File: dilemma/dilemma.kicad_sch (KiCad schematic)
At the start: 64 parts, among them J1 S3B-PH-SM4-TB(LF)(SN), J2 Serial, J3 BATTERY_CONN_DEANS, J5 S3B-PH-SM4-TB(LF)(SN), J7 trackball, SW1 SW_Push, SW10 SW_Push, SW11 SW_Push, SW12 SW_Push, SW13 SW_Push, SW14 SW_Push, SW15 SW_Push, SW16 SW_Push, SW17 SW_Push, SW2 SW_Push, SW26 SW_SPST, SW3 SW_Push, SW37 SW_SPST, SW4 SW_Push, SW5 SW_Push, SW6 SW_Push, SW7 SW_Push, SW8 SW_Push, SW9 SW_Push, U2 eliteC

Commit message: routing routing routing
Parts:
- removed H3: M4, footprints:MountingHole_3mm_Pad_thin, symbol Mechanical:MountingHole_Pad
- added R1: 5.1k, footprints:R_1206_handsolder, symbol Device:R
- R7: footprint footprints:R_1206_handsolder_reversible -> footprints:R_1206_handsolder
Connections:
- net GND: now also R1.2; no longer R7.1, U2.20 (F4)
- net row1_l: now also U2.17 (F7); no longer U2.19 (F5)
- net row4_l: now also U2.19 (F5); no longer U2.17 (F7)
- new net hand: R1.1, R7.1, U2.20 (F4)
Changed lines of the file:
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@@
   (junction (at 78.74 48.26) (diameter 0) (color 0 0 0 0)
+  )
+  (junction (at 51.435 152.4) (diameter 0) (color 0 0 0 0)
   )
   (no_connect (at 173.99 156.21))
@@
     (stroke (width 0) (type default) (color 0 0 0 0))
   )
-  (wire (pts (xy 69.85 156.972) (xy 69.85 162.052))
-    (stroke (width 0) (type default) (color 0 0 0 0))
-  )
   (wire (pts (xy 308.61 134.62) (xy 308.61 127))
     (stroke (width 0) (type default) (color 0 0 0 0))
@@
     (stroke (width 0) (type default) (color 0 0 0 0))
   )
-  (wire (pts (xy 46.482 152.4) (xy 51.562 152.4))
+  (wire (pts (xy 46.482 152.4) (xy 51.435 152.4))
     (stroke (width 0) (type default) (color 0 0 0 0))
   )
@@
     (stroke (width 0) (type default) (color 0 0 0 0))
   )
-  (wire (pts (xy 51.562 152.4) (xy 51.562 156.972))
+  (wire (pts (xy 51.435 152.4) (xy 51.435 158.75))
     (stroke (width 0) (type default) (color 0 0 0 0))
   )
@@
     (stroke (width 0) (type default) (color 0 0 0 0))
   )
+  (wire (pts (xy 60.325 158.75) (xy 69.85 158.75))
+    (stroke (width 0) (type default) (color 0 0 0 0))
+  )
   (wire (pts (xy 321.945 119.38) (xy 326.39 119.38))
+    (stroke (width 0) (type default) (color 0 0 0 0))
+  )
+  (wire (pts (xy 51.435 152.4) (xy 51.562 152.4))
     (stroke (width 0) (type default) (color 0 0 0 0))
   )
@@
     (stroke (width 0) (type default) (color 0 0 0 0))
   )
-  (wire (pts (xy 51.562 156.972) (xy 69.85 156.972))
-    (stroke (width 0) (type default) (color 0 0 0 0))
-  )
   (wire (pts (xy 327.66 134.62) (xy 327.66 99.06))
     (stroke (width 0) (type default) (color 0 0 0 0))
   )
   (wire (pts (xy 55.88 48.26) (xy 55.88 45.72))
+    (stroke (width 0) (type default) (color 0 0 0 0))
+  )
+  (wire (pts (xy 69.85 158.75) (xy 69.85 162.052))
     (stroke (width 0) (type default) (color 0 0 0 0))
   )
@@
   )
   (polyline (pts (xy 287.655 22.86) (xy 293.37 22.86))
+    (stroke (width 0) (type default) (color 0 0 0 0))
+  )
+  (wire (pts (xy 52.705 158.75) (xy 51.435 158.75))
     (stroke (width 0) (type default) (color 0 0 0 0))
   )
@@
     )
   )
-  (global_label "row1_l" (shape input) (at 73.66 111.76 0)
-    (effects (font (size 1.27 1.27)) (justify left))
-    (property "Intersheet References" "${INTERSHEET_REFS}" (id 0) (at 102.87 153.67 0)
+  (global_label "row1_l" (shape input) (at 73.66 116.84 0)
+    (effects (font (size 1.27 1.27)) (justify left))
+    (property "Intersheet References" "${INTERSHEET_REFS}" (id 0) (at 102.87 158.75 0)
       (effects (font (size 1.27 1.27)) hide)
     )
@@
     )
   )
-  (global_label "row4_l" (shape input) (at 73.66 116.84 0)
-    (effects (font (size 1.27 1.27)) (justify left))
-    (property "Intersheet References" "${INTERSHEET_REFS}" (id 0) (at 102.87 171.45 0)
+  (global_label "row4_l" (shape input) (at 73.66 111.76 0)
+    (effects (font (size 1.27 1.27)) (justify left))
+    (property "Intersheet References" "${INTERSHEET_REFS}" (id 0) (at 102.87 166.37 0)
       (effects (font (size 1.27 1.27)) hide)
     )
@@
       (effects (font (size 1.27 1.27)) (justify left))
     )
-    (property "Footprint" "footprints:R_1206_handsolder_reversible" (id 2) (at 55.372 154.178 90)
+    (property "Footprint" "footprints:R_1206_handsolder" (id 2) (at 55.372 154.178 90)
       (effects (font (size 1.27 1.27)) hide)
     )
@@
     (pin "2")
   )
+  (symbol (lib_id "Device:R") (at 56.515 158.75 90) (unit 1)
+    (in_bom yes) (on_board yes)
+    (property "Reference" "R1" (id 0) (at 55.245 156.21 0)
+      (effects (font (size 1.27 1.27)) (justify left))
+    )
+    (property "Value" "5.1k" (id 1) (at 57.785 156.21 0)
+      (effects (font (size 1.27 1.27)) (justify left))
+    )
+    (property "Footprint" "footprints:R_1206_handsolder" (id 2) (at 56.515 160.528 90)
+      (effects (font (size 1.27 1.27)) hide)
+    )
+    (property "Datasheet" "~" (id 3) (at 56.515 158.75 0)
+      (effects (font (size 1.27 1.27)) hide)
+    )
+    (property "JLCPCB BOM" "1" (id 4) (at 56.515 158.75 0)
+      (effects (font (size 1.27 1.27)) hide)
+    )
+    (property "JLCPCB Part" "C26033" (id 5) (at 56.515 158.75 0)
+      (effects (font (size 1.27 1.27)) hide)
+    )
+    (pin "1")
+    (pin "2")
+  )
   (symbol (lib_id "Device:D") (at 151.13 38.1 180) (unit 1)
     (in_bom yes) (on_board yes)
@@
     (pin "2")
   )
-  (symbol (lib_id "power:GND") (at 277.495 34.925 0) (unit 1)
-    (in_bom yes) (on_board yes)
-    (property "Reference" "#PWR0107" (id 0) (at 277.495 41.275 0)
-      (effects (font (size 1.27 1.27)) hide)
-    )
-    (property "Value" "GND" (id 1) (at 277.339 41.9099 90)
-      (effects (font (size 1.27 1.27)) (justify left))
-    )
-    (property "Footprint" "" (id 2) (at 277.495 34.925 0)
-      (effects (font (size 1.27 1.27)) hide)
-    )
-    (property "Datasheet" "" (id 3) (at 277.495 34.925 0)
-      (effects (font (size 1.27 1.27)) hide)
-    )
-    (pin "1")
-  )
   (symbol (lib_id "power:+5VL") (at 95.25 100.33 0) (unit 1)
     (in_bom yes) (on_board yes) (fields_autoplaced)
@@
     )
     (property "Datasheet" "" (id 3) (at 307.34 34.925 0)
-      (effects (font (size 1.27 1.27)) hide)
-    )
-    (pin "1")
-  )
-  (symbol (lib_id "Mechanical:MountingHole_Pad") (at 277.495 32.385 0) (unit 1)
-    (in_bom yes) (on_board yes)
-    (property "Reference" "H3" (id 0) (at 276.225 27.305 0)
-      (effects (font (size 1.27 1.27)) (justify left))
-    )
-    (property "Value" "M4" (id 1) (at 276.225 44.577 0)
-      (effects (font (size 1.27 1.27)) (justify left))
-    )
-    (property "Footprint" "footprints:MountingHole_3mm_Pad_thin" (id 2) (at 277.495 32.385 0)
-      (effects (font (size 1.27 1.27)) hide)
-    )
-    (property "Datasheet" "~" (id 3) (at 277.495 32.385 0)
       (effects (font (size 1.27 1.27)) hide)
     )
@@
       (reference "#PWR0106") (unit 1) (value "GND") (footprint "")
     )
-    (path "/7ee12246-48f8-49a8-bcd4-e3487c6db589"
-      (reference "#PWR0107") (unit 1) (value "GND") (footprint "")
-    )
     (path "/bacc65b4-66ed-4f84-a32f-72178fa6b135"
       (reference "D3") (unit 1) (value "D") (footprint "footprints:D_1206_handsolder_reversible")
@@
       (reference "H2") (unit 1) (value "M4") (footprint "footprints:MountingHole_3mm_Pad_thin")
     )
-    (path "/8f3d2726-b39f-482d-888f-43d8200309de"
-      (reference "H3") (unit 1) (value "M4") (footprint "footprints:MountingHole_3mm_Pad_thin")
-    )
     (path "/eab541c6-214e-4bdc-a65e-96cf56f5a486"
       (reference "H4") (unit 1) (value "M4") (footprint "footprints:MountingHole_3mm_Pad_thin")
@@
       (reference "PSW1") (unit 1) (value "SW_DPDT_x2") (footprint "local-libraries:Switch_MSK-12C01-07")
     )
+    (path "/4472aae1-b147-4122-a247-84cbdd93496c"
+      (reference "R1") (unit 1) (value "5.1k") (footprint "footprints:R_1206_handsolder")
+    )
     (path "/4acaff23-3513-4df1-ad8e-582535069bb0"
       (reference "R3") (unit 1) (value "4.7k") (footprint "footprints:R_1206_handsolder_reversible")
@@
     )
     (path "/230e74d0-be4c-4179-b8ac-0a56b1c74f86"
-      (reference "R7") (unit 1) (value "5.1k") (footprint "footprints:R_1206_handsolder_reversible")
+      (reference "R7") (unit 1) (value "5.1k") (footprint "footprints:R_1206_handsolder")
     )
     (path "/10c00776-633d-4d70-8200-26e4b25fd090"

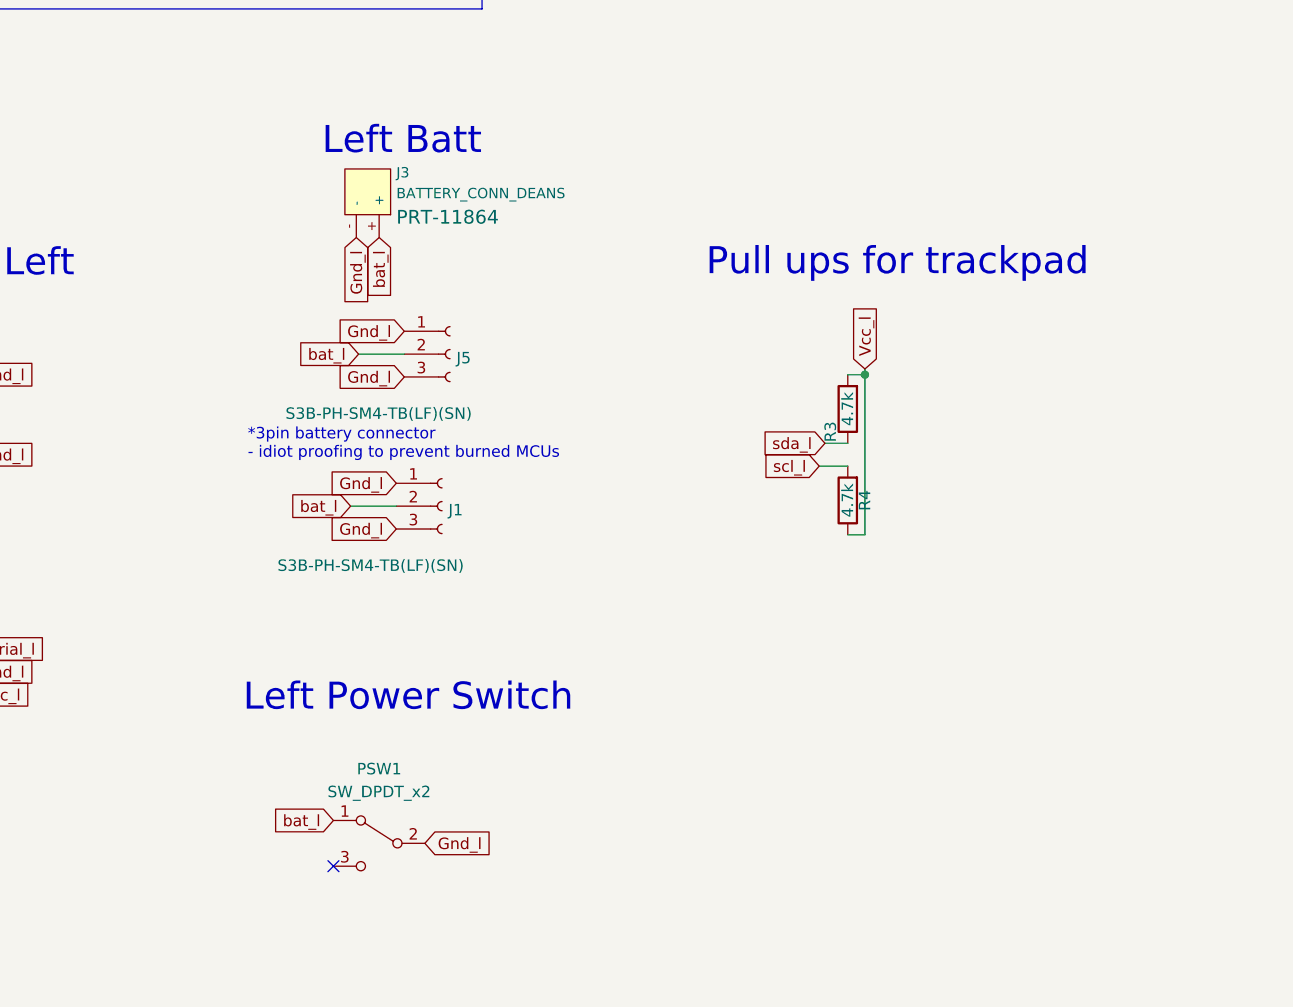
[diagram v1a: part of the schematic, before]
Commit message: Redid battery routing
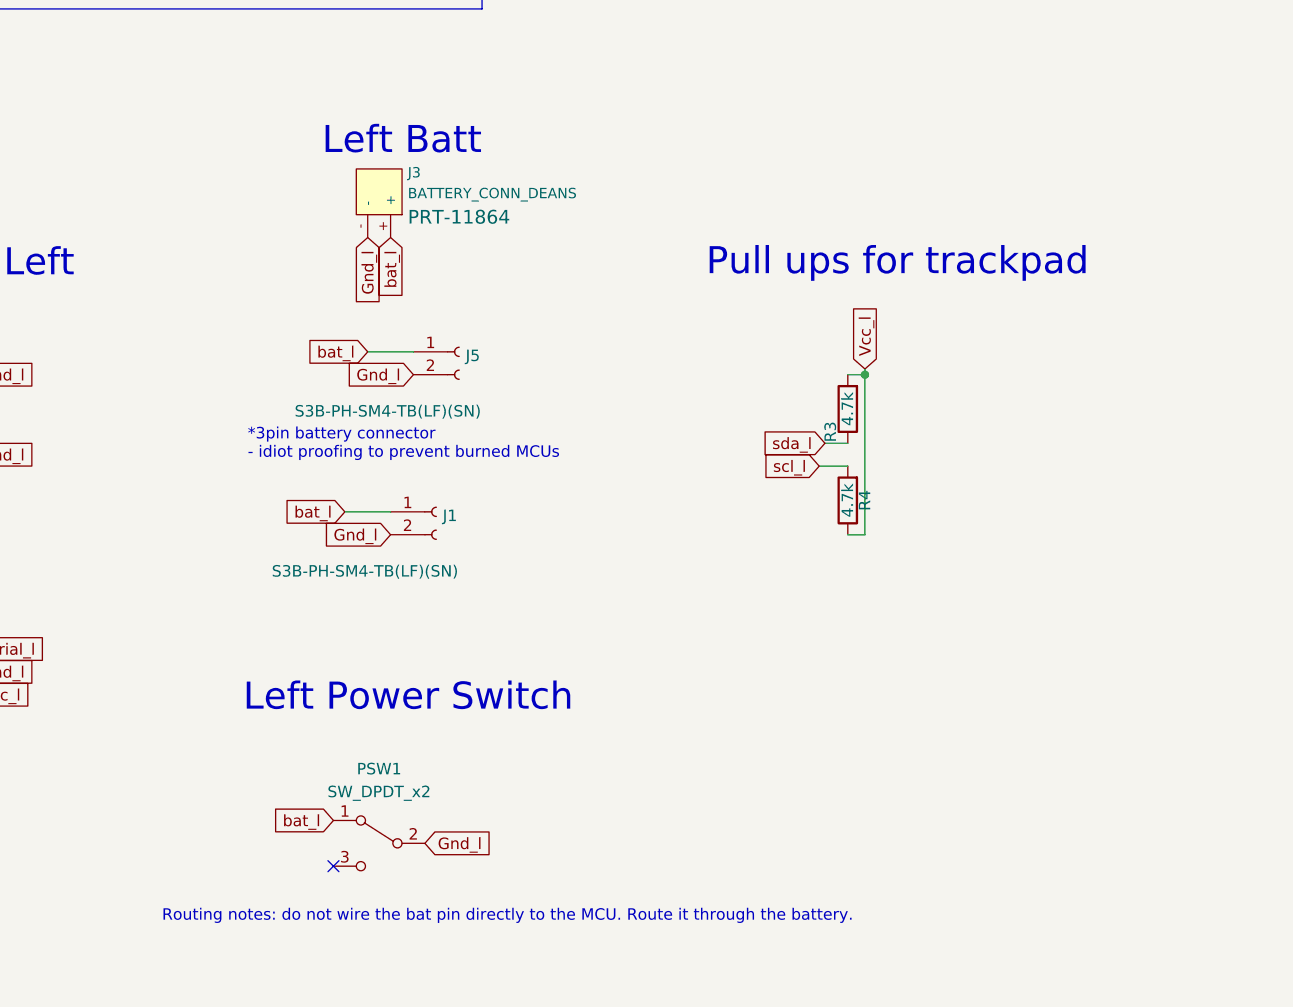
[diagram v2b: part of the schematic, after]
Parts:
- D10, D13, D14, D15, D18, D19, D20, D24, D25, D26, D3, D30, D33, D4, D5, D8, D9: footprint footprints:D_1206_handsolder_reversible -> local-libraries:D_1206_handsolder_reversible
- H1, H2, H4, H5, H6, H7, H8, H9: footprint footprints:MountingHole_3mm_Pad_thin -> local-libraries:MountingHole_3mm_Pad_thin
- J1, J5: footprint Connector_JST:JST_SH_BM03B-SRSS-TB_1x03-1MP_P1.00mm_Vertical -> local-libraries:JST_SH_BM02B-SRSS-TB_1x02-1MP_P1.00mm_Vertical; symbol Connector:Conn_01x03_Female -> Connector:Conn_01x02_Female
- J2: footprint footprints:Jack_3.5mm_PJ320E_Horizontal_reversible -> local-libraries:Jack_3.5mm_PJ320E_Horizontal_reversible
- JP1, JP2, JP3, JP4, JP5, JP6, JP7, JP8: footprint footprints:SolderJumper-2_P1.3mm_Open_RoundedPad1.0x1.5mm -> local-libraries:SolderJumper-2_P1.3mm_Open_RoundedPad1.0x1.5mm
- O2: footprint footprints:PinHeader_1x04_P2.54mm_Vertical -> local-libraries:PinHeader_1x04_P2.54mm_Vertical
- R3, R4: footprint footprints:R_1206_handsolder_reversible -> local-libraries:R_1206_handsolder_reversible
- SW1, SW10, SW11, SW12, SW13, SW14, SW15, SW16, SW17, SW2, SW3, SW4, SW5, SW6, SW7, SW8, SW9: footprint footprints:SW_MX_choc -> local-libraries:SW_MX_choc
- SW26, SW37: footprint footprints:SW_Push_1P1T_NO_6x6mm_H9.5mm -> local-libraries:SW_Push_1P1T_NO_6x6mm_H9.5mm
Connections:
- net GND: now also J1.2 (Pin_2), J5.2 (Pin_2); no longer J1.1 (Pin_1), J1.3 (Pin_3), J5.1 (Pin_1), J5.3 (Pin_3)
- net bat_l: now also J1.1 (Pin_1), J5.1 (Pin_1); no longer J1.2 (Pin_2), J5.2 (Pin_2)
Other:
- note added: "Routing notes: do not wire the bat pin directly to the MCU. Route it through the battery."
- moved on the sheet: J3

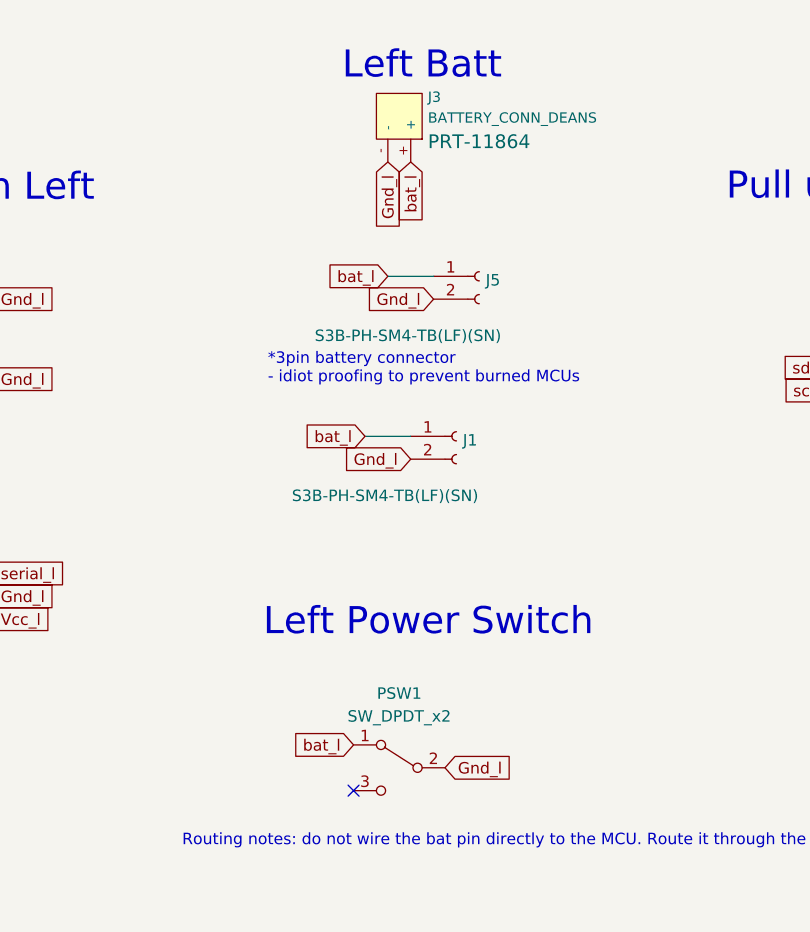
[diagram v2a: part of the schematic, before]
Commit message: fix power switch
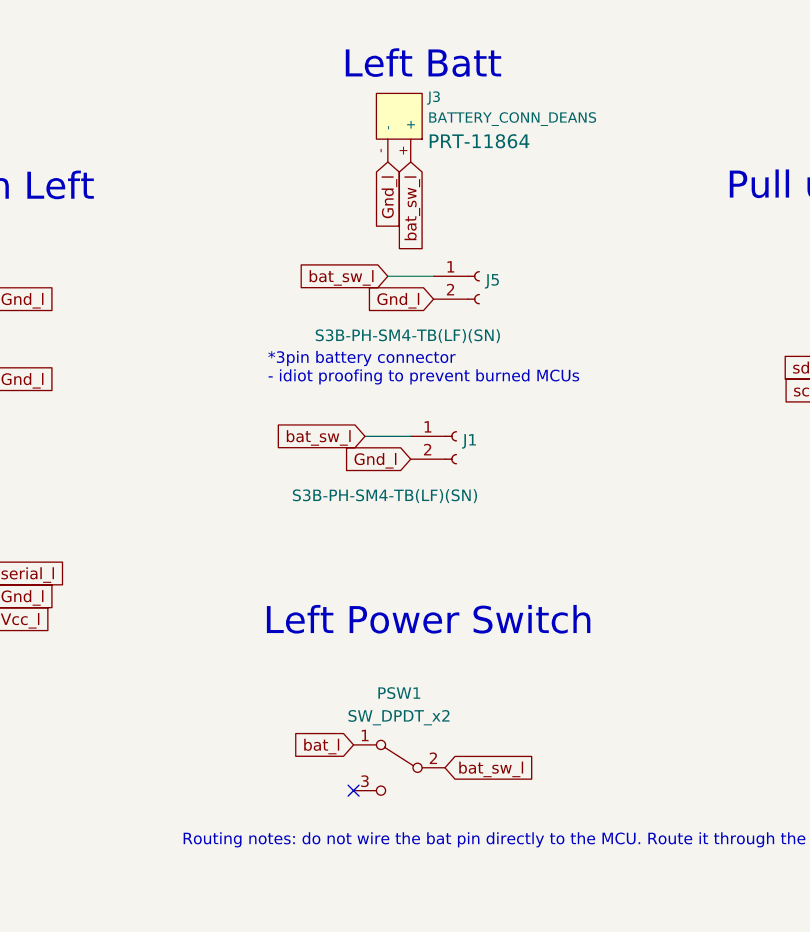
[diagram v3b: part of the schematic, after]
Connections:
- net GND: no longer PSW1.2 (B)
- net bat_l: no longer J1.1 (Pin_1), J3.+, J5.1 (Pin_1)
- new net bat_sw_l: J1.1 (Pin_1), J3.+, J5.1 (Pin_1), PSW1.2 (B)
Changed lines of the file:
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@@
+    )
+  )
+  (global_label "bat_sw_l" (shape input) (at 184.15 153.67 0)
+    (effects (font (size 1.27 1.27)) (justify left))
+    (property "Intersheet References" "${INTERSHEET_REFS}" (id 0) (at 60.96 22.86 0)
+      (effects (font (size 1.27 1.27)) hide)
     )
   )
@@
     (property "Intersheet References" "${INTERSHEET_REFS}" (id 0) (at 78.1293 127.0794 0)
       (effects (font (size 1.27 1.27)) (justify left) hide)
+    )
+  )
+  (global_label "bat_sw_l" (shape input) (at 180.34 86.36 270)
+    (effects (font (size 1.27 1.27)) (justify right))
+    (property "Intersheet References" "${INTERSHEET_REFS}" (id 0) (at 311.15 -36.83 0)
+      (effects (font (size 1.27 1.27)) hide)
     )
   )
@@
     )
   )
-  (global_label "bat_l" (shape input) (at 180.34 86.36 270)
-    (effects (font (size 1.27 1.27)) (justify right))
-    (property "Intersheet References" "${INTERSHEET_REFS}" (id 0) (at 311.15 -36.83 0)
-      (effects (font (size 1.27 1.27)) hide)
-    )
-  )
   (global_label "scl_l" (shape input) (at 227.965 111.76 180)
     (effects (font (size 1.27 1.27)) (justify right))
@@
     (effects (font (size 1.27 1.27)) (justify left))
     (property "Intersheet References" "${INTERSHEET_REFS}" (id 0) (at 10.16 64.77 0)
-      (effects (font (size 1.27 1.27)) hide)
-    )
-  )
-  (global_label "bat_l" (shape input) (at 175.26 116.84 180)
-    (effects (font (size 1.27 1.27)) (justify right))
-    (property "Intersheet References" "${INTERSHEET_REFS}" (id 0) (at 298.45 247.65 0)
       (effects (font (size 1.27 1.27)) hide)
     )
@@
     )
   )
-  (global_label "bat_l" (shape input) (at 177.8 99.06 180)
+  (global_label "bat_sw_l" (shape input) (at 175.26 116.84 180)
+    (effects (font (size 1.27 1.27)) (justify right))
+    (property "Intersheet References" "${INTERSHEET_REFS}" (id 0) (at 298.45 247.65 0)
+      (effects (font (size 1.27 1.27)) hide)
+    )
+  )
+  (global_label "bat_sw_l" (shape input) (at 177.8 99.06 180)
     (effects (font (size 1.27 1.27)) (justify right))
     (property "Intersheet References" "${INTERSHEET_REFS}" (id 0) (at 300.99 229.87 0)
@@
     )
   )
-  (global_label "Gnd_l" (shape input) (at 184.15 153.67 0)
-    (effects (font (size 1.27 1.27)) (justify left))
-    (property "Intersheet References" "${INTERSHEET_REFS}" (id 0) (at 60.96 83.82 0)
-      (effects (font (size 1.27 1.27)) hide)
-    )
-  )
